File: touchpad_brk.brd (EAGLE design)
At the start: 39.4 x 42.9 mm, 3 parts

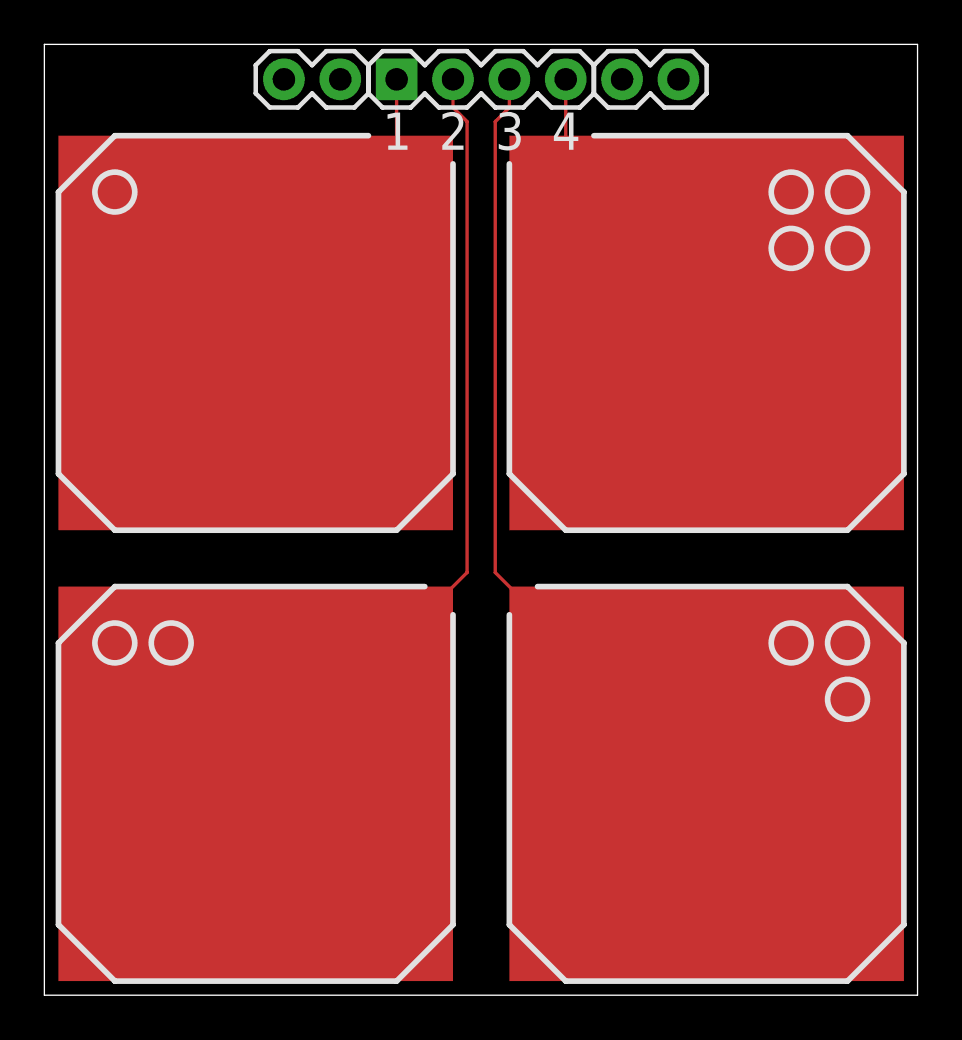
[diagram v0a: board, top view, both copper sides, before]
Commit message: Fixes: smaller pads, no grounding pins.
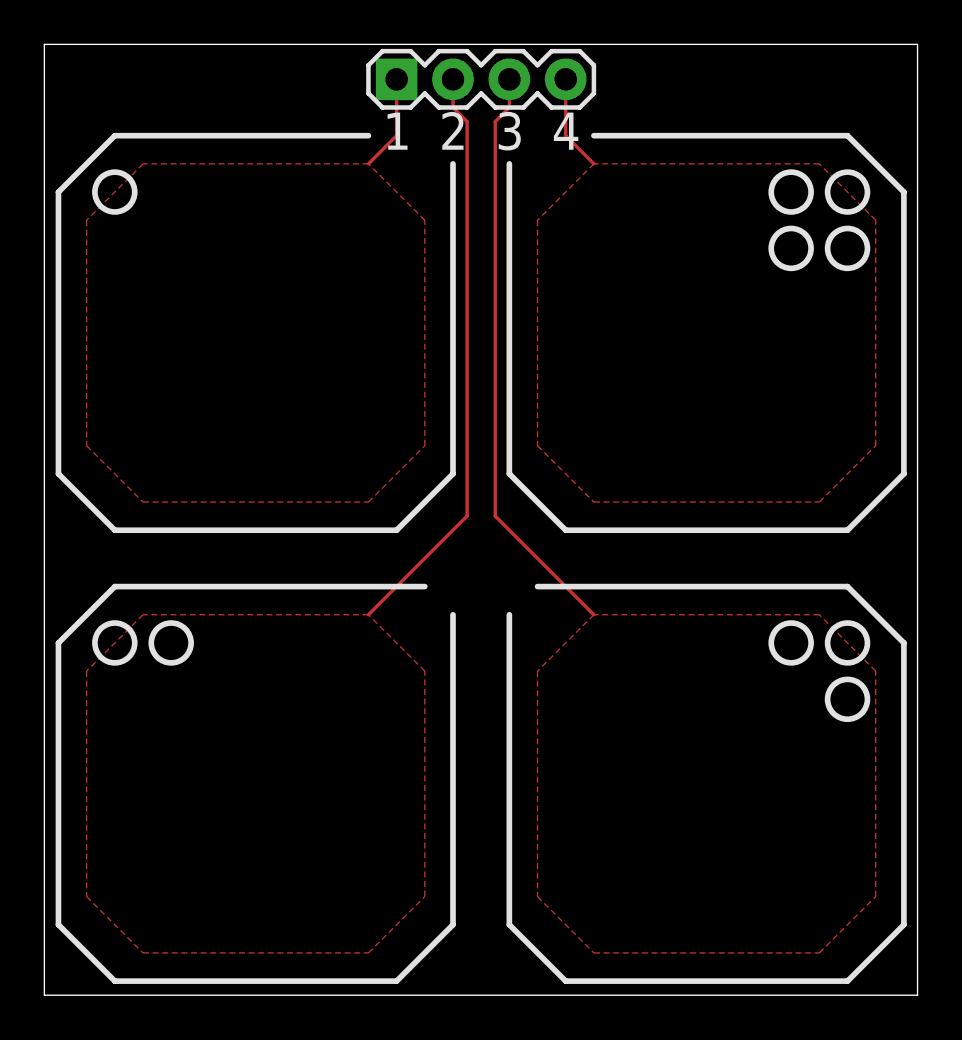
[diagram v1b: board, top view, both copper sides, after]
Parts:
- removed J2, J3: (no value), SparkFun-Connectors:1X02
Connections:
- removed net GND: J2.1, J2.2, J3.1, J3.2
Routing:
- net PAD4: track 3.17 -> 4.34 mm
- net PAD1: track 3.17 -> 4.34 mm
- net PAD3: track 25.2 -> 26.2 mm
- net PAD2: track 25.2 -> 26.2 mm
- added copper zone on layer 1, net PAD1
- added copper zone on layer 1, net PAD2
- added copper zone on layer 1, net PAD3
- added copper zone on layer 1, net PAD4
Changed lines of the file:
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@@
 <wire x1="41.255" y1="44.755" x2="1.905" y2="44.755" width="0" layer="20"/>
 <wire x1="1.905" y1="44.755" x2="1.905" y2="1.905" width="0" layer="20"/>
-<rectangle x1="2.54" y1="22.86" x2="20.32" y2="40.64" layer="1"/>
-<rectangle x1="22.86" y1="22.86" x2="40.64" y2="40.64" layer="1"/>
-<rectangle x1="2.54" y1="2.54" x2="20.32" y2="20.32" layer="1"/>
-<rectangle x1="22.86" y1="2.54" x2="40.64" y2="20.32" layer="1"/>
 <text x="17.145" y="40.005" size="1.6764" layer="25" font="vector">1</text>
 <text x="19.685" y="40.005" size="1.6764" layer="25" font="vector">2</text>
@@
 <attribute name="VALUE" x="16.51" y="40.005" size="1.27" layer="27"/>
 </element>
-<element name="J2" library="SparkFun-Connectors" package="1X02" value="" x="12.7" y="43.18" smashed="yes">
-<attribute name="VALUE" x="11.43" y="40.005" size="1.27" layer="27"/>
-</element>
-<element name="J3" library="SparkFun-Connectors" package="1X02" value="" x="27.94" y="43.18" smashed="yes">
-<attribute name="VALUE" x="26.67" y="40.005" size="1.27" layer="27"/>
-</element>
 </elements>
 <signals>
 <signal name="PAD4">
 <contactref element="J1" pad="4"/>
-<wire x1="25.4" y1="40.005" x2="25.4" y2="43.18" width="0.1524" layer="1"/>
+<polygon width="0.1524" layer="1">
+<vertex x="26.67" y="39.37"/>
+<vertex x="24.13" y="36.83"/>
+<vertex x="24.13" y="26.67"/>
+<vertex x="26.67" y="24.13"/>
+<vertex x="36.83" y="24.13"/>
+<vertex x="39.37" y="26.67"/>
+<vertex x="39.37" y="36.83"/>
+<vertex x="36.83" y="39.37"/>
+</polygon>
+<wire x1="25.4" y1="43.18" x2="25.4" y2="40.64" width="0.1524" layer="1"/>
+<wire x1="25.4" y1="40.64" x2="26.67" y2="39.37" width="0.1524" layer="1"/>
 </signal>
 <signal name="PAD1">
 <contactref element="J1" pad="1"/>
-<wire x1="17.78" y1="40.005" x2="17.78" y2="43.18" width="0.1524" layer="1"/>
+<polygon width="0.1524" layer="1">
+<vertex x="6.35" y="39.37"/>
+<vertex x="3.81" y="36.83"/>
+<vertex x="3.81" y="26.67"/>
+<vertex x="6.35" y="24.13"/>
+<vertex x="16.51" y="24.13"/>
+<vertex x="19.05" y="26.67"/>
+<vertex x="19.05" y="36.83"/>
+<vertex x="16.51" y="39.37"/>
+</polygon>
+<wire x1="17.78" y1="43.18" x2="17.78" y2="40.64" width="0.1524" layer="1"/>
+<wire x1="17.78" y1="40.64" x2="16.51" y2="39.37" width="0.1524" layer="1"/>
 </signal>
 <signal name="PAD2">
-<wire x1="19.05" y1="19.05" x2="20.955" y2="20.955" width="0.1524" layer="1"/>
-<wire x1="20.955" y1="20.955" x2="20.955" y2="41.275" width="0.1524" layer="1"/>
-<wire x1="20.955" y1="41.275" x2="20.32" y2="41.91" width="0.1524" layer="1"/>
+<wire x1="20.32" y1="41.91" x2="20.955" y2="41.275" width="0.1524" layer="1"/>
 <contactref element="J1" pad="2"/>
 <wire x1="20.32" y1="41.91" x2="20.32" y2="43.18" width="0.1524" layer="1"/>
+<polygon width="0.1524" layer="1">
+<vertex x="6.35" y="19.05"/>
+<vertex x="3.81" y="16.51"/>
+<vertex x="3.81" y="6.35"/>
+<vertex x="6.35" y="3.81"/>
+<vertex x="16.51" y="3.81"/>
+<vertex x="19.05" y="6.35"/>
+<vertex x="19.05" y="16.51"/>
+<vertex x="16.51" y="19.05"/>
+</polygon>
+<wire x1="20.955" y1="41.275" x2="20.955" y2="23.495" width="0.1524" layer="1"/>
+<wire x1="20.955" y1="23.495" x2="16.51" y2="19.05" width="0.1524" layer="1"/>
 </signal>
 <signal name="PAD3">
-<wire x1="24.13" y1="19.05" x2="22.225" y2="20.955" width="0.1524" layer="1"/>
-<wire x1="22.225" y1="20.955" x2="22.225" y2="41.275" width="0.1524" layer="1"/>
-<wire x1="22.225" y1="41.275" x2="22.86" y2="41.91" width="0.1524" layer="1"/>
+<wire x1="22.86" y1="41.91" x2="22.225" y2="41.275" width="0.1524" layer="1"/>
 <contactref element="J1" pad="3"/>
 <wire x1="22.86" y1="41.91" x2="22.86" y2="43.18" width="0.1524" layer="1"/>
-</signal>
-<signal name="GND">
-<contactref element="J2" pad="2"/>
-<contactref element="J2" pad="1"/>
-<contactref element="J3" pad="2"/>
-<contactref element="J3" pad="1"/>
-<wire x1="27.94" y1="43.18" x2="30.48" y2="43.18" width="0" layer="19" extent="1-1"/>
-<wire x1="15.24" y1="43.18" x2="27.94" y2="43.18" width="0" layer="19" extent="1-1"/>
-<wire x1="12.7" y1="43.18" x2="15.24" y2="43.18" width="0" layer="19" extent="1-1"/>
+<polygon width="0.1524" layer="1">
+<vertex x="26.67" y="19.05"/>
+<vertex x="24.13" y="16.51"/>
+<vertex x="24.13" y="6.35"/>
+<vertex x="26.67" y="3.81"/>
+<vertex x="36.83" y="3.81"/>
+<vertex x="39.37" y="6.35"/>
+<vertex x="39.37" y="16.51"/>
+<vertex x="36.83" y="19.05"/>
+</polygon>
+<wire x1="22.225" y1="41.275" x2="22.225" y2="23.495" width="0.1524" layer="1"/>
+<wire x1="22.225" y1="23.495" x2="26.67" y2="19.05" width="0.1524" layer="1"/>
 </signal>
 </signals>
